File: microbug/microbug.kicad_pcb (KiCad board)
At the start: 2 copper layers, 31.7 x 38.1 mm, 26 parts, among them J1 Conn_01x04, J2 Conn_01x03, J3 Conn_01x02, M1 Motor_DC, M2 Motor_DC, U1 ATtiny1616-S, U2 QRE1113GR, U3 QRE1113GR, U5 TC78H660FNG

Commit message: new layout edits, still missing logo
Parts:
- D1, D3: footprint LED_SMD:LED_0603_1608Metric_Pad1.05x0.95mm_HandSolder -> LED_THT:LED_D3.0mm
- moved C2 1.28 mm to (79.5, 69.1)
- moved C3 1.28 mm to (77.9, 69.1)
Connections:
- M2 pad 1: Net-(M2-Pad1) -> Net-(U5-Pad9)
- U5 pad 10: Net-(M2-Pad1) -> Net-(M2-Pad2)
- U5 pad 9: Net-(M2-Pad2) -> Net-(U5-Pad9)
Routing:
- net Net-(M2-Pad1): track 14.4 -> 0.00 mm
- net GND: track 13.8 -> 2.55 mm, vias 6 -> 7
- net Net-(U5-Pad9): track 0.00 -> 9.87 mm
- net Net-(D1-Pad2): track 14.8 -> 12.5 mm, vias 2 -> 1
- net Net-(D3-Pad2): track 14.9 -> 12.9 mm, vias 2 -> 1
- net /OUT1: track 27.5 -> 25.5 mm
- net +3V3: track 73.0 -> 74.6 mm
- net /PWM1: track 13.5 -> 14.8 mm
- net /DIR1: track 18.8 -> 18.0 mm
- net Net-(M1-Pad1): track 7.85 -> 8.50 mm
- net Net-(R9-Pad2): track 6.53 -> 5.98 mm
- net Net-(M1-Pad2): track 5.79 -> 6.32 mm

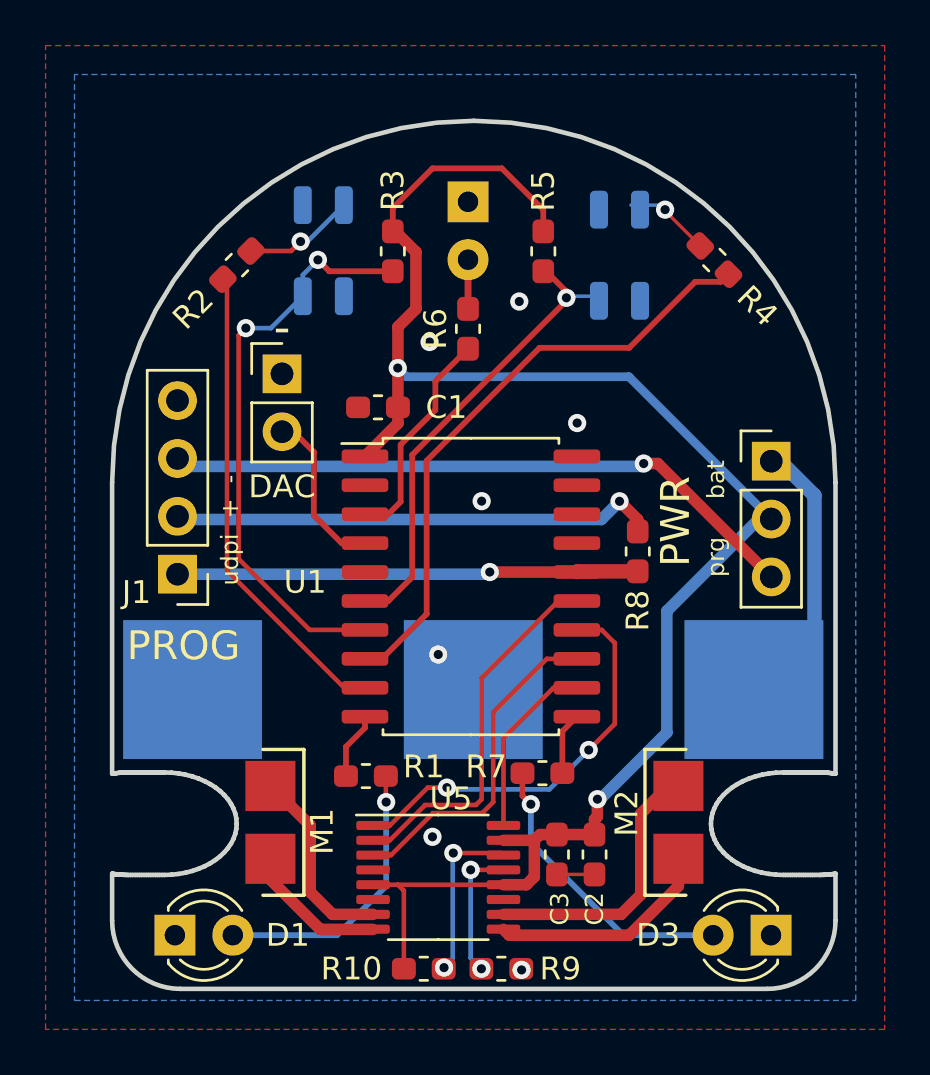
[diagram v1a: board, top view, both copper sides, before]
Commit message: bug gets new connector, logo silk, small changes
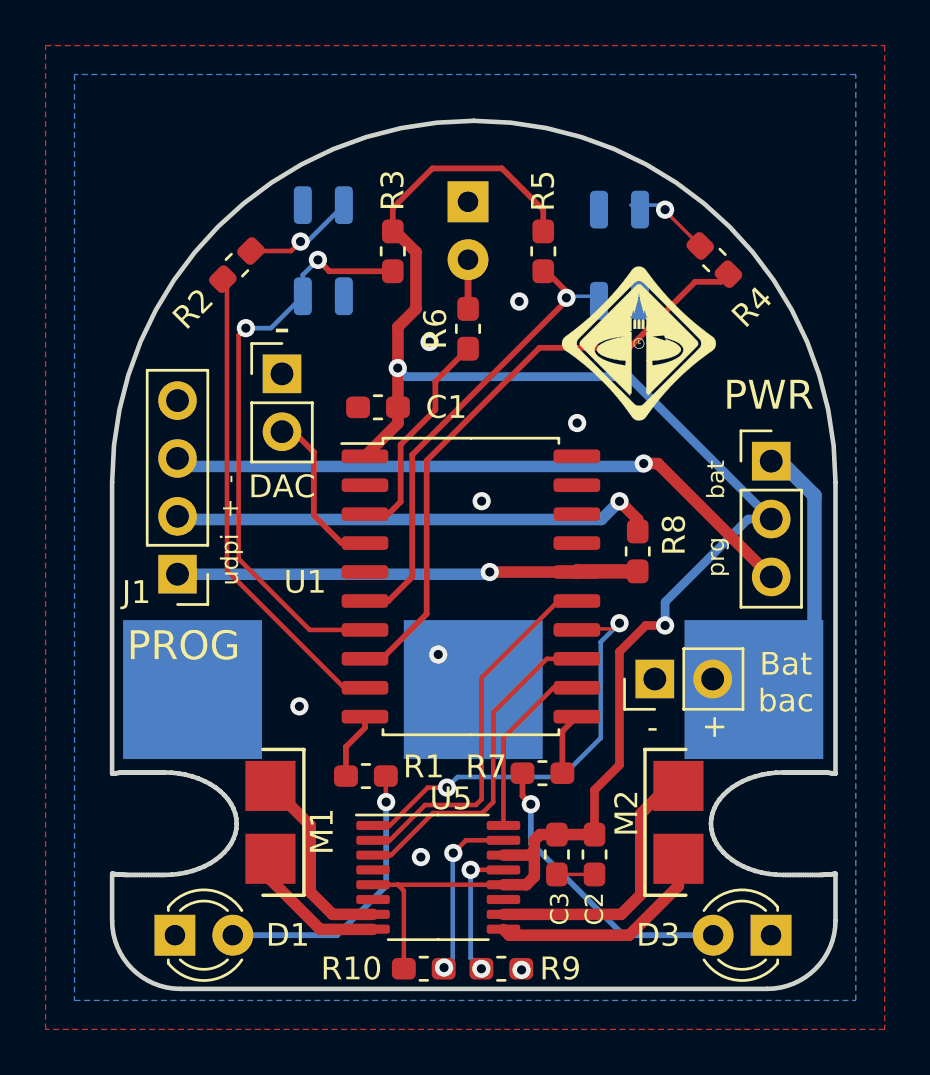
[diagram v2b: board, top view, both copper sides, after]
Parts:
- added G***: LOGO, microbug-fplib:ieee-logo, F.Cu at (81.5, 46.7)
- added J4: Conn_01x02, Connector_PinHeader_2.54mm:PinHeader_1x02_P2.54mm_Vertical, F.Cu at (82.2, 61.4)
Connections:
- net Net-(BT1-Pad1) renamed /V_bat
- R10 pad 2: Net-(R10-Pad2) -> Net-(U5-Pad15)
- U5 pad 14: Net-(R10-Pad2) -> +3V3
- U5 pad 15: +3V3 -> Net-(U5-Pad15)
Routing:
- net Net-(U5-Pad15): track 0.00 -> 7.69 mm, vias 0 -> 2
- net Net-(R10-Pad2): track 7.49 -> 0.00 mm, vias 2 -> 0
- net /DIR1: track 18.0 -> 19.0 mm
- net +3V3: track 74.6 -> 75.4 mm
- net GND: vias 7 -> 8
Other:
- board text added: "+"
- board text added: "BAC logo?"
- board text added: "Bat bac"

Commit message: Update silkscreen for prog header
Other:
- board text added: "RX TX + -"
- board text removed: "udpi + -"
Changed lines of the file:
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@@
     (effects (font (size 0.762 0.762) (thickness 0.1905)))
   )
-  (gr_text "udpi  +  -" (at 63.5 54.864 90) (layer "F.SilkS")
+  (gr_text "RX  TX  +   -" (at 63.5 53.34 90) (layer "F.SilkS")
     (effects (font (size 0.762 0.762) (thickness 0.1905)))
   )

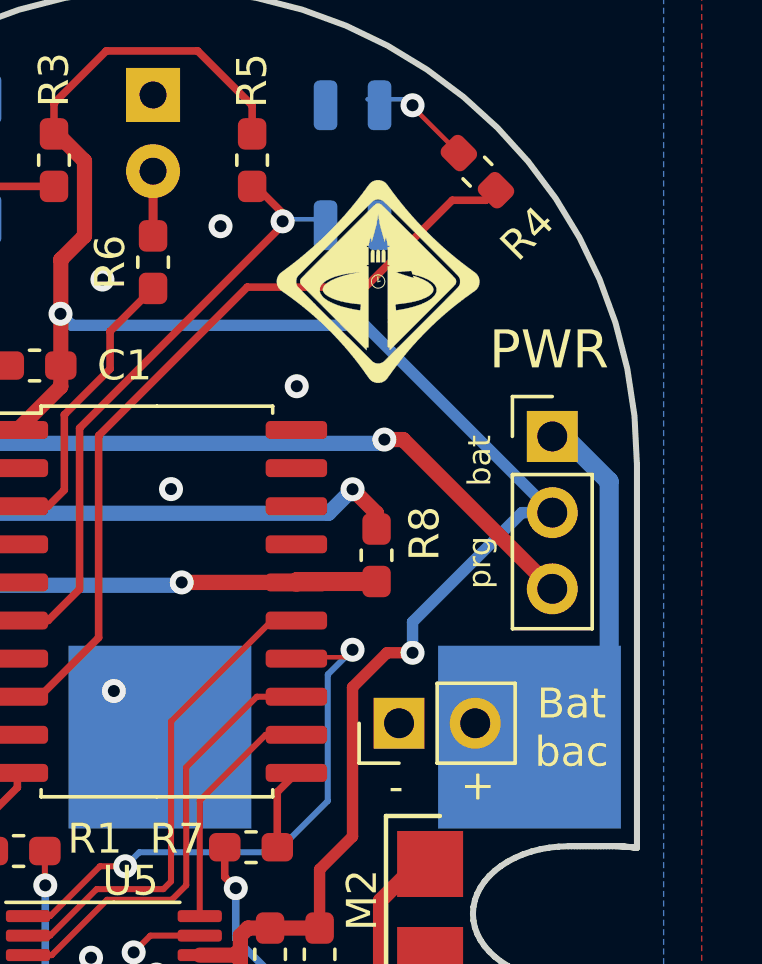
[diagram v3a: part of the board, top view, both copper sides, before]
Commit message: mbug logos and reorientation of extra power pins
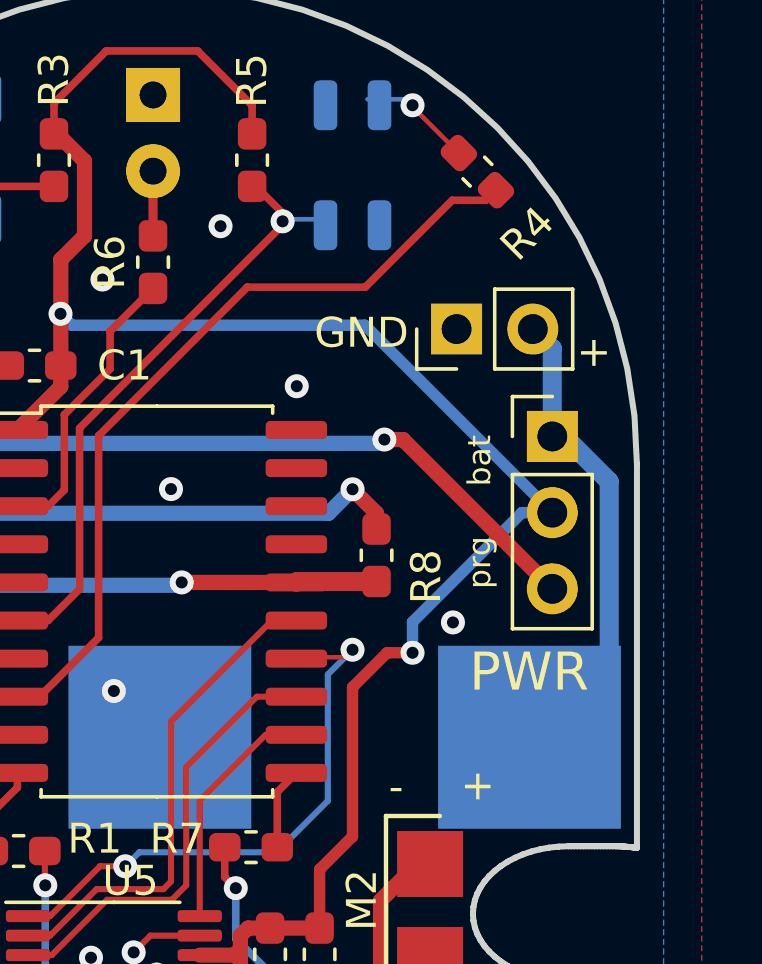
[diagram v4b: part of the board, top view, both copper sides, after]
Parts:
- added G***: LOGO, microbug-fplib:bac-logo, B.Cu at (79.9, 70.4)
- G***: moved to B.Cu
- moved G*** 27.4 mm to (67.7, 70.4), turned to 180 degrees
- moved J4 13.3 mm to (84.1, 48.3)
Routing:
- net /V_bat: track 12.1 -> 16.0 mm
- net GND: vias 8 -> 9
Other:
- board text added: "GND"
- board text added: "microbug v0.1"
- board text removed: "BAC logo?"
- board text removed: "Bat bac"
- board text removed: "microbug v0"

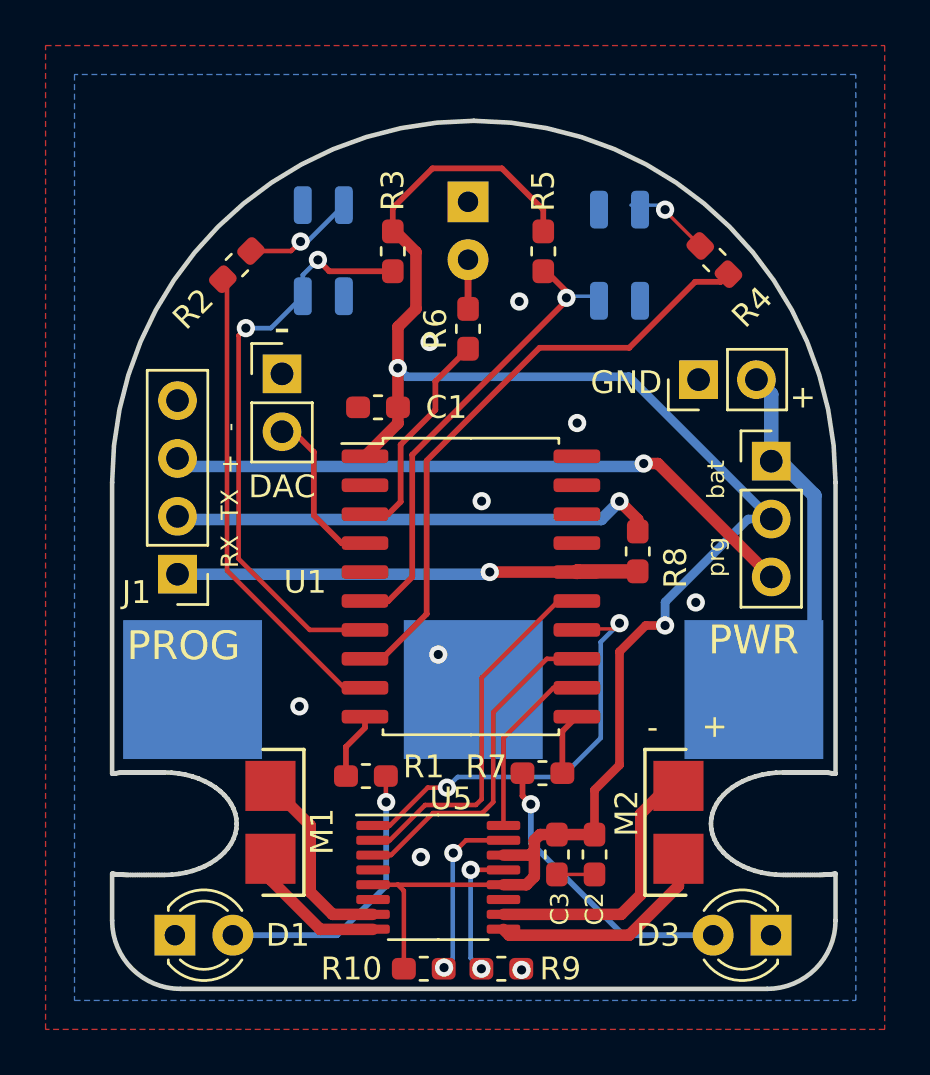
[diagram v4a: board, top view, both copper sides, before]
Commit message: BAC DFM clean
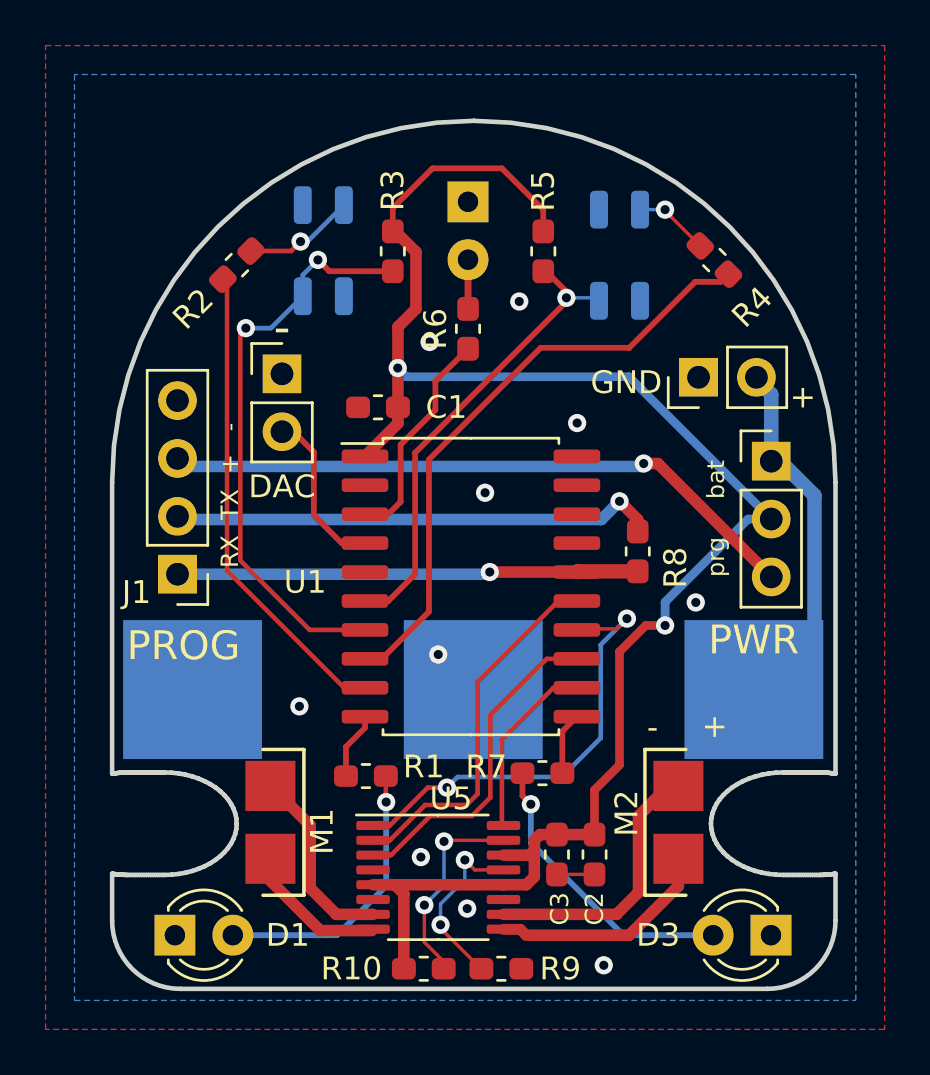
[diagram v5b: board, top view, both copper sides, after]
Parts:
- moved J4 0.10 mm to (84.1, 48.2)
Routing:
- net Net-(R9-Pad2): track 5.98 -> 7.84 mm
- net Net-(U5-Pad15): track 7.69 -> 8.93 mm
- net /DIR1: track 19.0 -> 19.7 mm
- net GND: track 2.55 -> 2.50 mm, vias 9 -> 10
